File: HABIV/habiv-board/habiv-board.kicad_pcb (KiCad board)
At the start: 4 copper layers, 114 parts, among them IC1 RTC_PCF8523T, J1 Micro_SD_Card_Det, J10 Conn_01x08_Male, J2 Conn_ARM_JTAG_SWD_20, J3 Conn_01x02_Male, J4 Conn_01x16_Male, J5 Conn_01x02_Male, J6 Conn_01x16_Male, J7 Conn_01x16_Male, J8 Conn_01x08_Male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

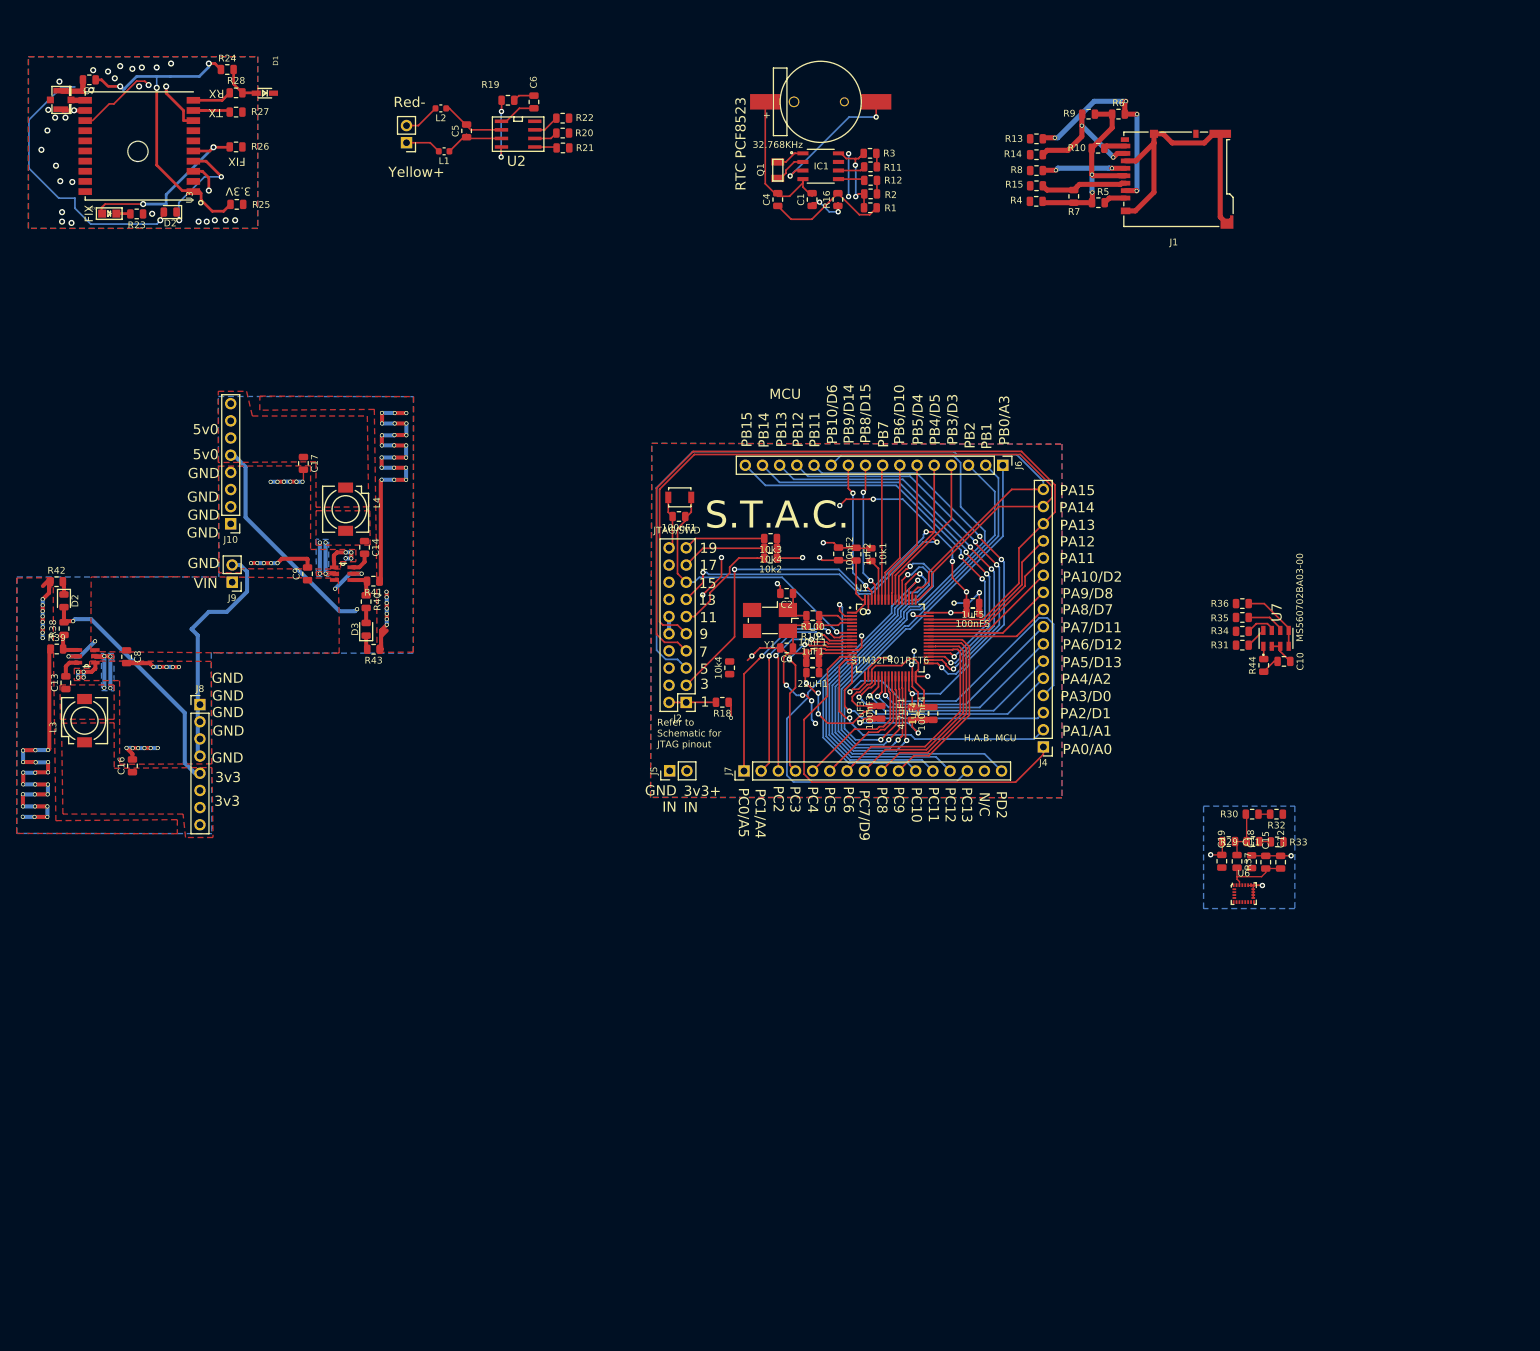
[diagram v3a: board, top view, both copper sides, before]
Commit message: clean up silkscreen
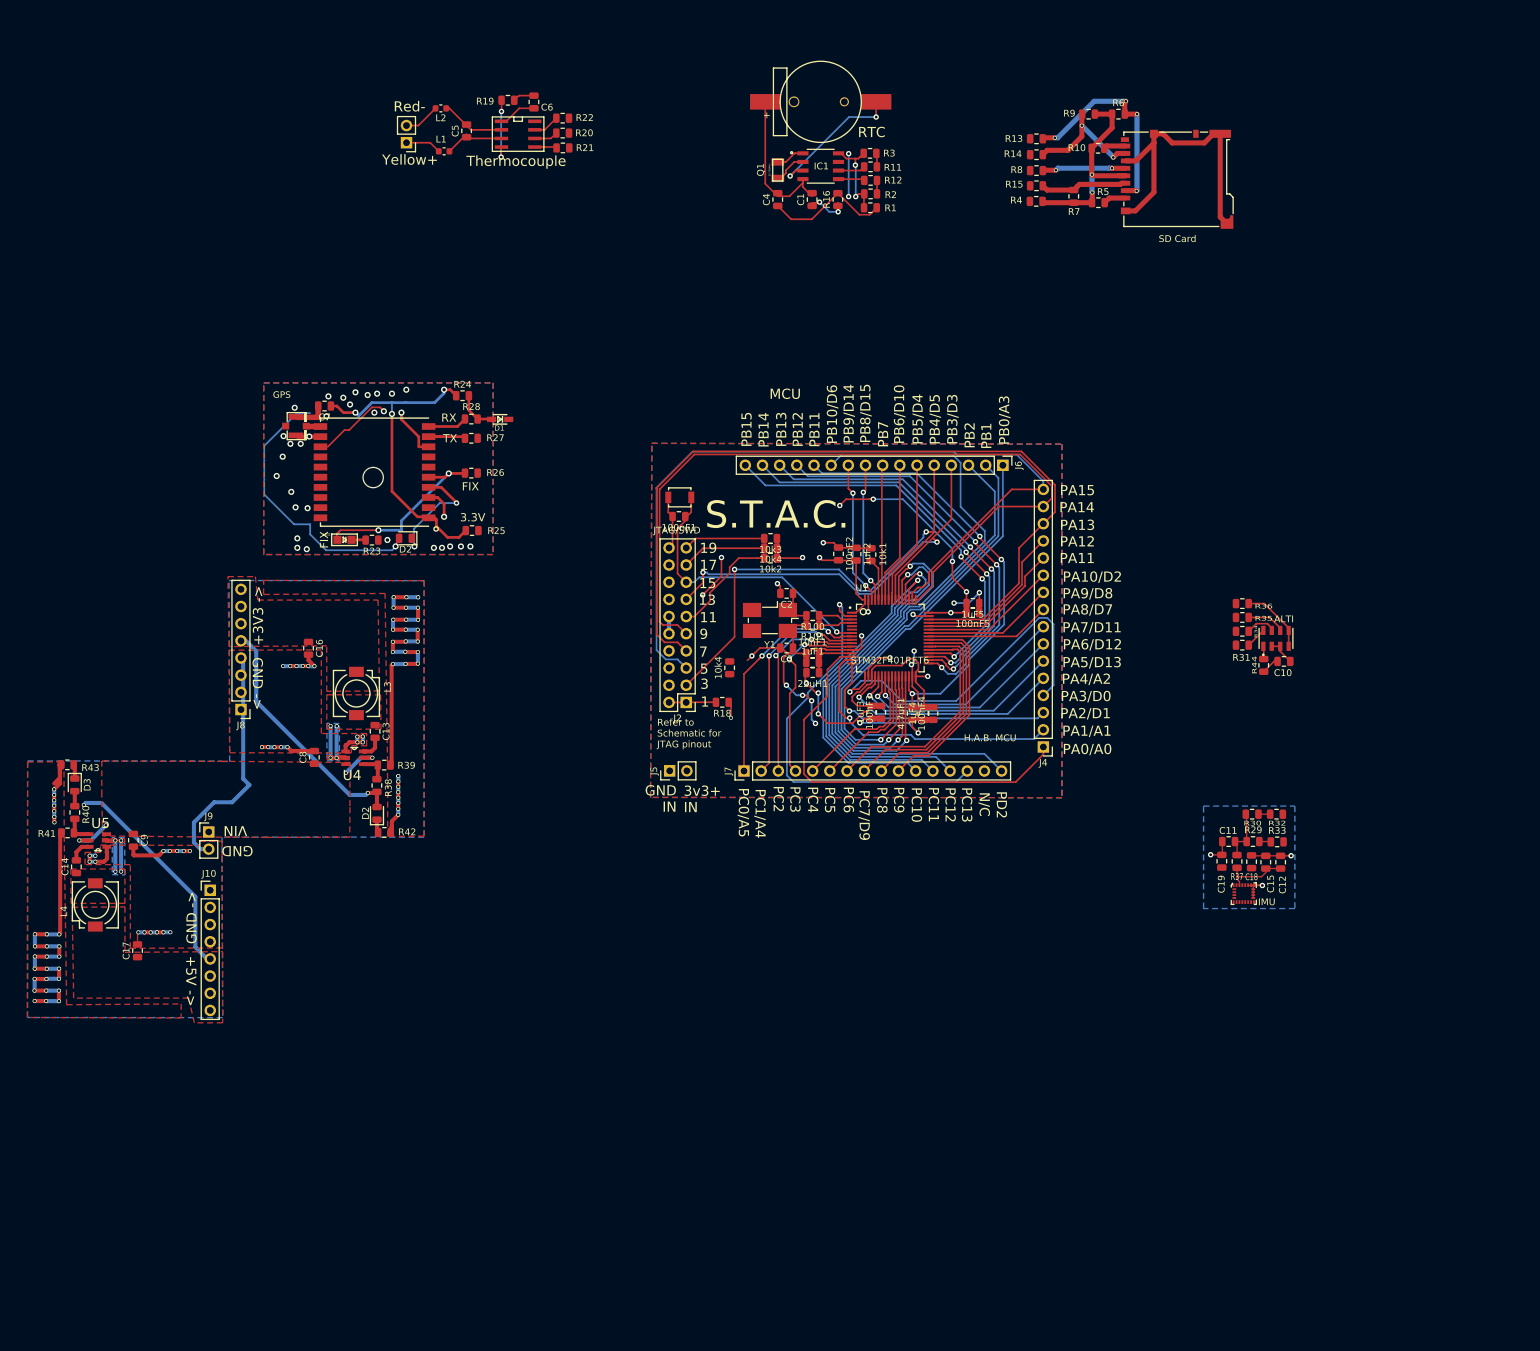
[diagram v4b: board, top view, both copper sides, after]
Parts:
- SD Card: renamed from J1
- U7: value MS560702BA03-00 -> ALTI
- moved C17 76.2 mm to (32.6, 147.5), turned to 90 degrees
- moved L4 69.3 mm to (26.2, 140.6), turned to 90 degrees
- moved C14 63.6 mm to (23.5, 135.0), turned to 90 degrees
- moved R42 61.1 mm to (69.1, 129.9), turned to 180 degrees
- moved D2 59.5 mm to (72.2, 86.4)
- moved R27 59.5 mm to (81.9, 71.7)
- moved C7 59.5 mm to (60.2, 66.9)
- moved D1 59.5 mm to (86.2, 68.8)
- moved GPS 59.5 mm to (67.6, 76.7)
- moved R23 59.5 mm to (67.2, 86.7)
- moved R24 59.5 mm to (80.6, 65.3)
- moved R25 59.5 mm to (82.0, 85.3)
- moved R26 59.5 mm to (81.9, 76.8)
- moved R28 59.5 mm to (81.9, 68.8)
- moved LED1 59.5 mm to (63.2, 86.7)
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- renumbered U3 to GPS, U6 to IMU, U2 to Thermocouple
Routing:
- net GND: track 427.0 -> 425.8 mm
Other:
- board text added: "+3V3 ->"
- board text added: "+5V ->"
- board text added: "GND ->"
- board text added: "RTC"
- board text added: "U4"
- board text added: "U5"
- board text removed: "3v3"
- board text removed: "5v0"
- board text removed: "RTC PCF8523"

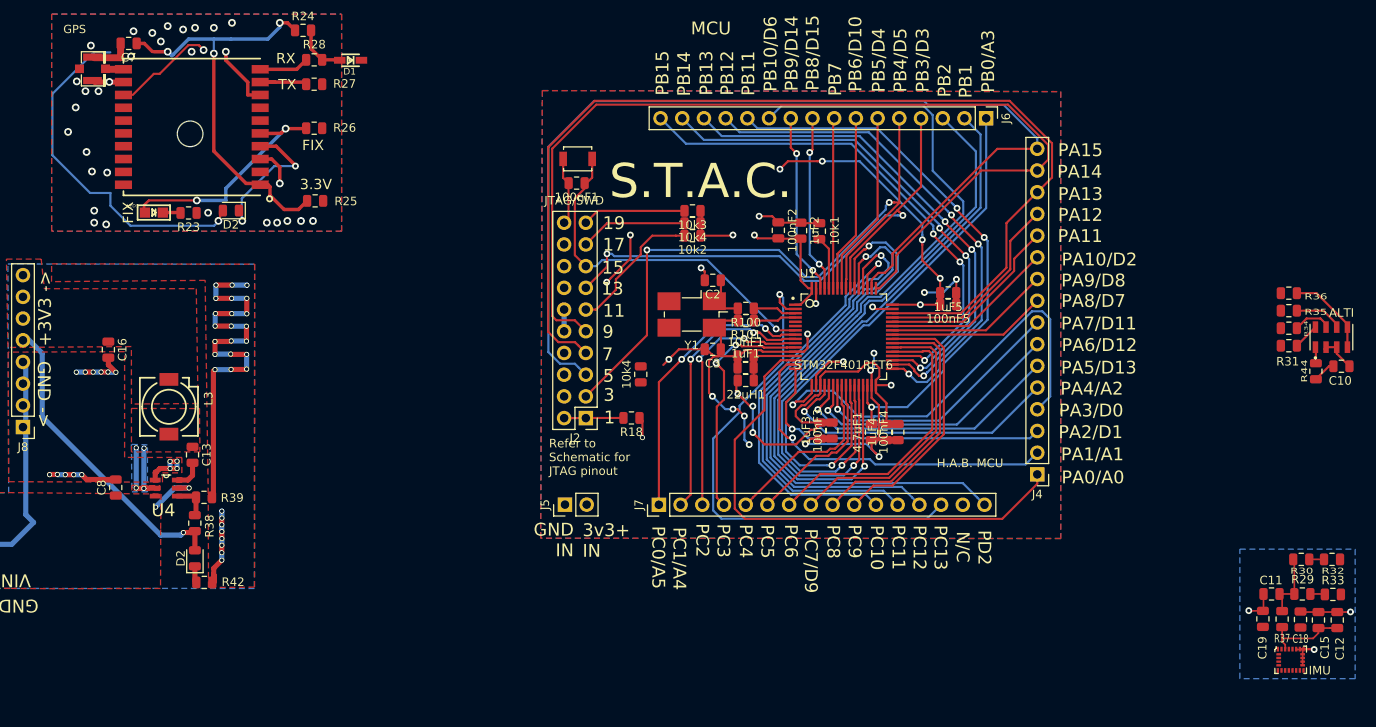
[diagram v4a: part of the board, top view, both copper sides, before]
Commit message: fix gps and fix imu connections
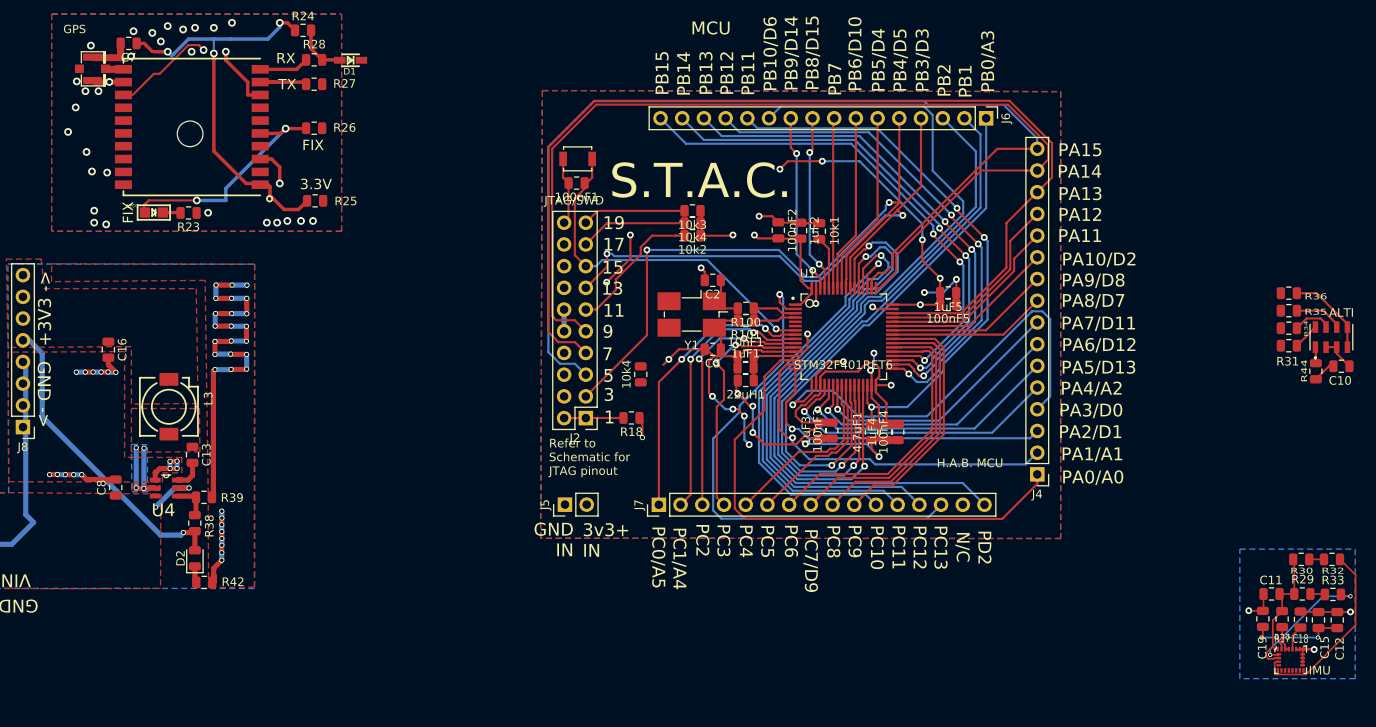
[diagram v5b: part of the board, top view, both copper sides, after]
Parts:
- removed the D2 at (72.2, 86.4)
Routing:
- net +3V3: track 191.1 -> 158.2 mm, vias 13 -> 12
- net Net-(R32-Pad1): track 0.00 -> 22.2 mm
- net (no net): track 22.3 -> 6.70 mm, vias 4 -> 2
- net Net-(R33-Pad1): track 0.00 -> 14.9 mm, vias 0 -> 2
- net Net-(C19-Pad2): track 0.00 -> 4.73 mm, vias 0 -> 2
- net Net-(C18-Pad1): track 0.00 -> 2.91 mm
- net Net-(C12-Pad1): track 10.0 -> 10.7 mm, vias 0 -> 2
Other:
- net class Default: clearance 0.2 -> 0.1; trace_width 0.6 -> 0.2; via_dia 0.8 -> 0.5; via_drill 0.4 -> 0.3
- rule trace_clearance: 0.2 -> 0.1
